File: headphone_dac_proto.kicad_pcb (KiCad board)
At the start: 2 copper layers, 75.5 x 55.5 mm, 61 parts, among them J1 USB_B_Mini, J2 Conn_02x10_Odd_Even, J3 Conn_02x05_Odd_Even, J4 Conn_01x06_Male, J5 Conn_01x06, J6 6.35mm, U1 LT3042xMSE, U2 CY8C5888LTI-LP097, U3 CS4344, U4 TPA6139A2, Y1 Crystal_GND24

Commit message: Change to 4 layer board
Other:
- copper layers 2 -> 4

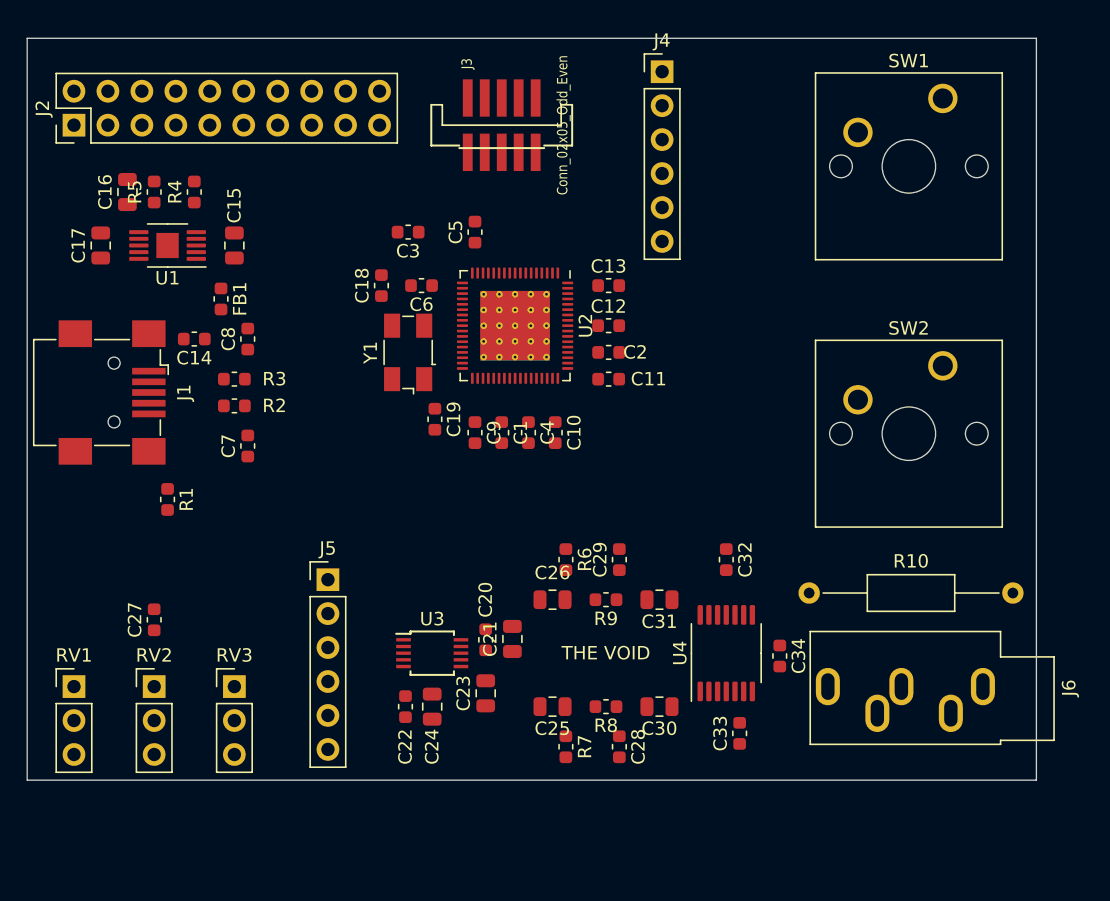
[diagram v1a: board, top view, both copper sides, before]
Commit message: Change peripheral switches and pots
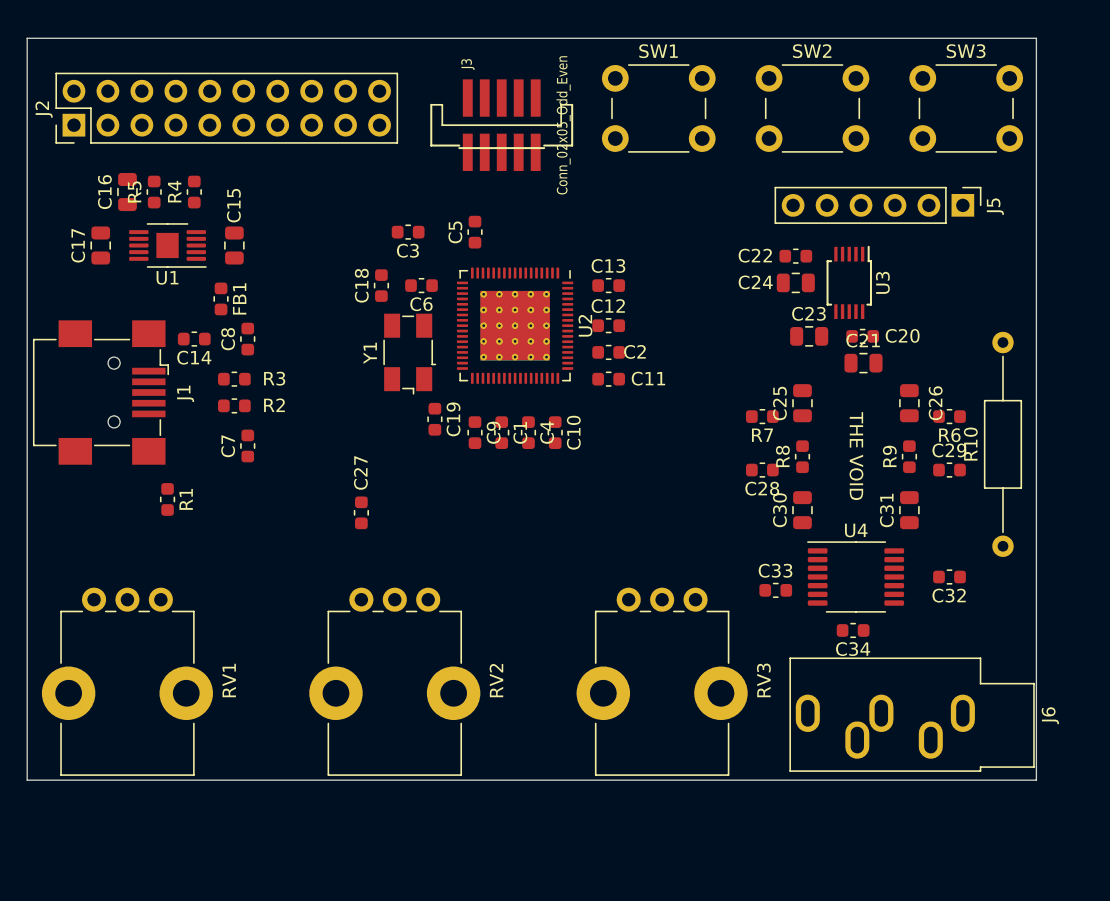
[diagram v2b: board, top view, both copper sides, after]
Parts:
- removed J4: Conn_01x06_Male, Connector_PinHeader_2.54mm:PinHeader_1x06_P2.54mm_Vertical
- added SW3: ~, Button_Switch_THT:SW_PUSH_6mm_H5mm, F.Cu at (155.5, 95.5)
- RV1, RV2, RV3: footprint Connector_PinHeader_2.54mm:PinHeader_1x03_P2.54mm_Vertical -> Potentiometer_THT:Potentiometer_Bourns_PTV09A-1_Single_Vertical
- SW1, SW2: footprint Button_Switch_Keyboard:SW_Cherry_MX_1.00u_PCB -> Button_Switch_THT:SW_PUSH_6mm_H5mm
- moved J5 55.1 mm to (158.5, 105.0), turned to 270 degrees
- moved C22 44.6 mm to (146.0, 108.8), turned to 180 degrees
- moved C24 41.8 mm to (146.0, 110.8), turned to 180 degrees
- moved U3 41.7 mm to (150.0, 110.8), turned to 270 degrees
- moved C20 36.2 mm to (151.0, 114.8), turned to 0 degrees
- moved C23 36.0 mm to (147.0, 114.8), turned to 0 degrees
- moved C21 33.4 mm to (151.1, 116.8), turned to 0 degrees
- moved R6 30.6 mm to (157.5, 120.8), turned to 180 degrees
- moved C26 30.5 mm to (154.5, 119.8), turned to 90 degrees
- moved RV3 30.2 mm to (133.5, 134.5), turned to 270 degrees
- moved C25 29.4 mm to (146.5, 119.8), turned to 90 degrees
- moved R7 28.7 mm to (143.5, 120.8), turned to 180 degrees
- moved C29 25.6 mm to (157.5, 124.8), turned to 0 degrees
- moved SW2 25.1 mm to (144.0, 95.5)
- moved R9 25.1 mm to (154.5, 123.8), turned to 90 degrees
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
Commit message: Change all the things
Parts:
- added C35: 1uF, Capacitor_SMD:C_0603_1608Metric, F.Cu at (113.5, 131.5)
- added C36: 1uF, Capacitor_SMD:C_0603_1608Metric, F.Cu at (133.5, 131.5)
- moved C27 20.3 mm to (93.5, 131.5)
- moved SW1 7.91 mm to (139.0, 100.0), turned to 180 degrees
- moved SW3 7.91 mm to (162.0, 100.0), turned to 180 degrees

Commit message: Placement is complete. Actually though.
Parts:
- added H1: ~, MountingHole:MountingHole_3mm_Pad_Via, F.Cu at (92.0, 151.5)
- added H2: ~, MountingHole:MountingHole_3mm_Pad, F.Cu at (92.0, 96.0)
- added H3: ~, MountingHole:MountingHole_3mm_Pad, F.Cu at (160.5, 96.0)
- added H4: ~, MountingHole:MountingHole_3mm_Pad, F.Cu at (160.5, 151.5)
- SW1, SW2, SW3: footprint Button_Switch_THT:SW_PUSH_6mm_H5mm -> Button_Switch_THT:SW_PUSH_6mm_H13mm
- moved J5 20.7 mm to (139.0, 112.0)
- moved J3 13.4 mm to (114.5, 108.5), turned to 0 degrees
- moved C5 9.82 mm to (119.5, 116.5)
- moved C27 9.22 mm to (99.5, 138.5)
- moved RV1 9.22 mm to (99.5, 141.5)
- moved C1 9.01 mm to (123.5, 131.0)
- moved C10 9.01 mm to (127.5, 131.0)
- moved C11 9.01 mm to (131.5, 127.0)
- moved C12 9.01 mm to (131.5, 123.0)
- moved C13 9.01 mm to (131.5, 120.0)
- moved C18 9.01 mm to (114.5, 120.0)
- moved C19 9.01 mm to (118.5, 130.0)
- moved C2 9.01 mm to (131.5, 125.0)
- moved C3 9.01 mm to (116.5, 116.0)
- moved C4 9.01 mm to (125.5, 131.0)
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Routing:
- added copper zone on In2.Cu, net +3V3
- added copper zone on In1.Cu, net GND
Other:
- board size 75.5 x 55.5 mm -> 75.5 x 62.5 mm

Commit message: I'm sorry Jackson. Please don't read these commit messages
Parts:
- removed J5: Conn_01x06, Connector_PinHeader_2.54mm:PinHeader_1x06_P2.54mm_Vertical
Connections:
- net /i2s_sdi renamed Net-(U2-Pad53)
- SW1 pad 1: Net-(SW1-Pad1) -> /sw1
- SW2 pad 2: Net-(SW2-Pad2) -> /sw2
- SW3 pad 1: Net-(SW3-Pad1) -> /sw3
- U2 pad 1: /bt_rts -> /i2s_sck
- U2 pad 2: /bt_rx -> /i2s_sdo
- U2 pad 3: Net-(SW1-Pad1) -> /sw2
- U2 pad 4: Net-(SW2-Pad2) -> /sw1
- U2 pad 48: /i2s_mck -> Net-(U2-Pad48)
- U2 pad 49: /i2s_lrck -> Net-(U2-Pad49)
- U2 pad 50: /i2s_sck -> Net-(U2-Pad50)
- U2 pad 51: /i2s_sdo -> Net-(U2-Pad51)
- U2 pad 61: Net-(SW3-Pad1) -> Net-(U2-Pad61)
- U2 pad 66: /bt_cts -> /i2s_mck
- U2 pad 68: /bt_tx -> /i2s_lrck
- U3 pad 1: /i2s_sd -> /i2s_sdo

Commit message: Started routing
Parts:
- moved U3 11.8 mm to (138.3, 109.5), turned to 0 degrees
- moved C22 10.8 mm to (136.3, 113.5), turned to 270 degrees
- moved C21 10.8 mm to (144.3, 108.4), turned to 90 degrees
- moved C20 10.7 mm to (142.3, 108.5), turned to 90 degrees
- moved C24 8.16 mm to (138.3, 113.5), turned to 270 degrees
- moved C23 5.23 mm to (142.3, 112.5), turned to 90 degrees
- moved C13 2.26 mm to (131.8, 117.8), turned to 90 degrees
- moved C10 2.25 mm to (125.2, 131.0)
- moved C18 2.14 mm to (116.5, 120.8), turned to 0 degrees
- moved C19 2.14 mm to (116.5, 129.2), turned to 180 degrees
- moved C12 1.60 mm to (132.5, 124.2)
- moved C4 1.50 mm to (127.0, 131.0)
- moved C2 1.41 mm to (132.5, 126.0)
- moved C3 1.27 mm to (116.8, 117.2)
- moved C11 1.25 mm to (132.5, 127.8)
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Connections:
- C27 pad 1: Net-(C27-Pad1) -> /as
- C35 pad 1: Net-(C27-Pad1) -> /as
- C36 pad 1: Net-(C27-Pad1) -> /as
- RV1 pad 1: Net-(C27-Pad1) -> /as
- RV2 pad 1: Net-(C27-Pad1) -> /as
- RV3 pad 1: Net-(C27-Pad1) -> /as
- U2 pad 3: /sw2 -> /bt_tx
- U2 pad 33: /a2 -> /as
- U2 pad 34: /a1 -> /a0
- U2 pad 36: /a0 -> /a1
- U2 pad 37: Net-(C27-Pad1) -> /a2
- U2 pad 4: /sw1 -> /bt_rx
- U2 pad 61: Net-(U2-Pad61) -> /bt_cts
- U2 pad 62: /ft_~rts~ -> /bt_rts
- U2 pad 63: /ft_rx -> /sw3
- U2 pad 64: /ft_tx -> /sw2
- U2 pad 65: /ft_~cts~ -> /sw1
- U4 pad 8: Net-(U4-Pad7) -> Net-(U4-Pad8)
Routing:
- net /sw3: track 0.00 -> 39.6 mm, vias 0 -> 1
- net /bt_cts: track 0.00 -> 38.4 mm, vias 0 -> 1
- net /bt_rts: track 0.00 -> 37.8 mm, vias 0 -> 1
- net +3V3: track 0.00 -> 37.1 mm, vias 0 -> 5
- net GND: track 0.00 -> 35.6 mm, vias 0 -> 1
- net /bt_rx: track 0.00 -> 32.5 mm
- net /bt_tx: track 0.00 -> 30.6 mm
- net /sw2: track 0.00 -> 28.6 mm, vias 0 -> 1
- net /sw1: track 0.00 -> 27.8 mm, vias 0 -> 1
- net /~mute~: track 0.00 -> 24.5 mm
- net /vccd: track 0.00 -> 20.0 mm, vias 0 -> 2
- net /usb_d+: track 0.00 -> 18.1 mm, vias 0 -> 2
- net /usb_d-: track 0.00 -> 17.3 mm, vias 0 -> 2
- net /i2s_mck: track 0.00 -> 17.1 mm
- net /i2s_sdo: track 0.00 -> 14.9 mm
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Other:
- net class Default: trace_width 0.25 -> 0.2; via_dia 0.8 -> 0.6; via_drill 0.4 -> 0.3
- rule pad_to_mask_clearance: 0.05 -> 0.038
- rule trace_min: 0.2 -> 0.15
- rule via_min_size: 0.4 -> 0.6

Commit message: ERC and DRC passing
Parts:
- U1: footprint Package_SO:MSOP-10-1EP_3x3mm_P0.5mm_EP1.68x1.88mm -> Package_SO:MSOP-10-1EP_3x3mm_P0.5mm_EP1.68x1.88mm_ThermalVias
- moved R6 14.0 mm to (143.5, 120.8), turned to 0 degrees
- moved R7 13.8 mm to (157.2, 120.8), turned to 0 degrees
- moved R5 4.25 mm to (94.2, 106.0)
- moved C16 4.14 mm to (92.2, 105.8)
- moved C32 2.44 mm to (155.8, 134.5), turned to 90 degrees
- moved C27 2.06 mm to (101.5, 139.0), turned to 0 degrees
- moved J3 2.02 mm to (113.5, 110.2)
- moved C9 1.80 mm to (120.8, 129.5)
- moved C23 1.72 mm to (140.8, 113.2)
- moved FB1 1.35 mm to (101.8, 112.5)
- moved C17 1.25 mm to (94.0, 109.2), turned to 180 degrees
- moved C33 1.22 mm to (145.5, 134.5), turned to 90 degrees
- turned C28 to 0 degrees
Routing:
- net /as: track 0.00 -> 72.5 mm
- net GND: track 35.6 -> 102.6 mm, vias 1 -> 41
- net +3V3: track 37.1 -> 74.5 mm, vias 5 -> 12
- net Net-(J6-PadT): track 0.00 -> 28.3 mm
- net /a2: track 0.00 -> 27.2 mm
- net /a0: track 0.00 -> 26.4 mm
- net /xres: track 0.00 -> 26.1 mm
- net Net-(J1-Pad6): track 0.00 -> 23.2 mm
- net Net-(J6-PadR): track 0.00 -> 23.1 mm
- net Net-(C26-Pad2): track 0.00 -> 21.8 mm
- net /tms: track 0.00 -> 16.3 mm
- net /a1: track 0.00 -> 15.7 mm
- net /tck: track 0.00 -> 15.3 mm
- net /tdo: track 0.00 -> 14.0 mm
- net /tdi: track 0.00 -> 12.9 mm
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- added copper zone on F.Cu, net +3V3
- added copper zone on F.Cu, net +5V
- added copper zone on B.Cu, net GND

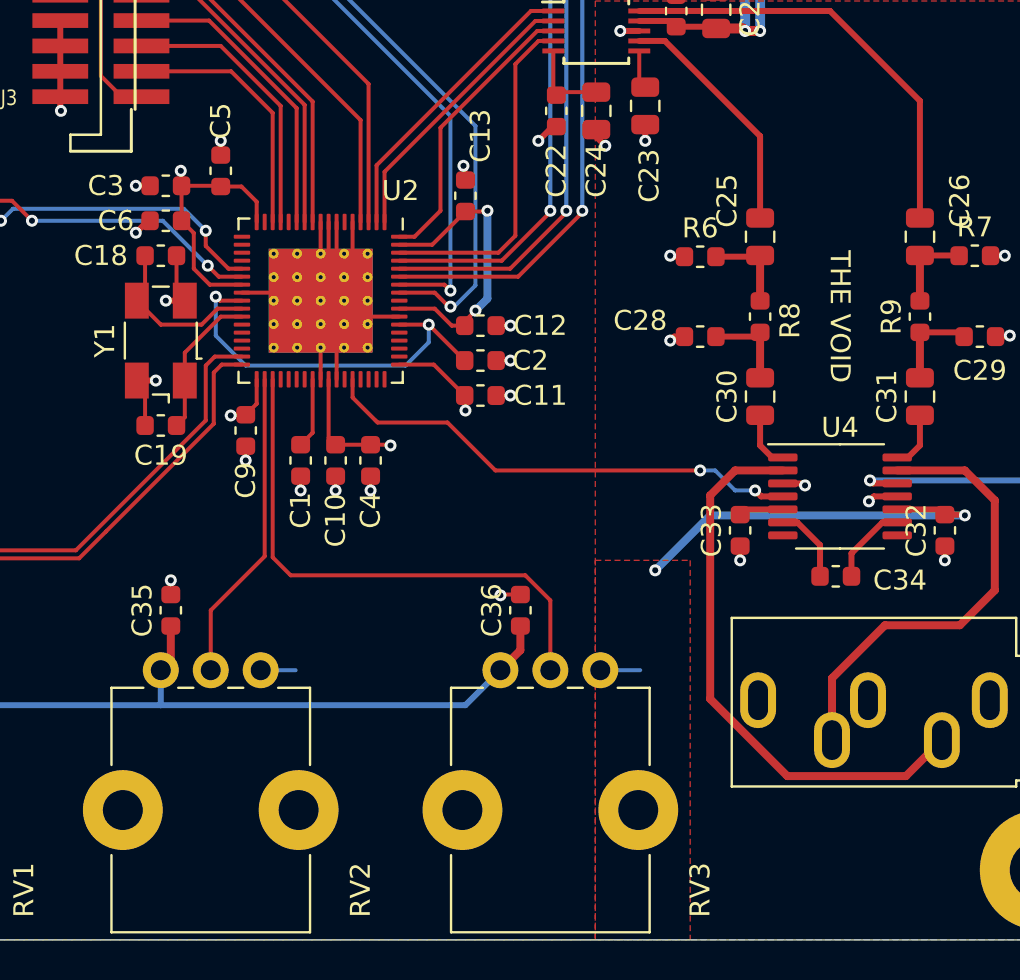
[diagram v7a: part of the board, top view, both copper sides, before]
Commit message: Switch to two layers. ERC, DRC passing agaom
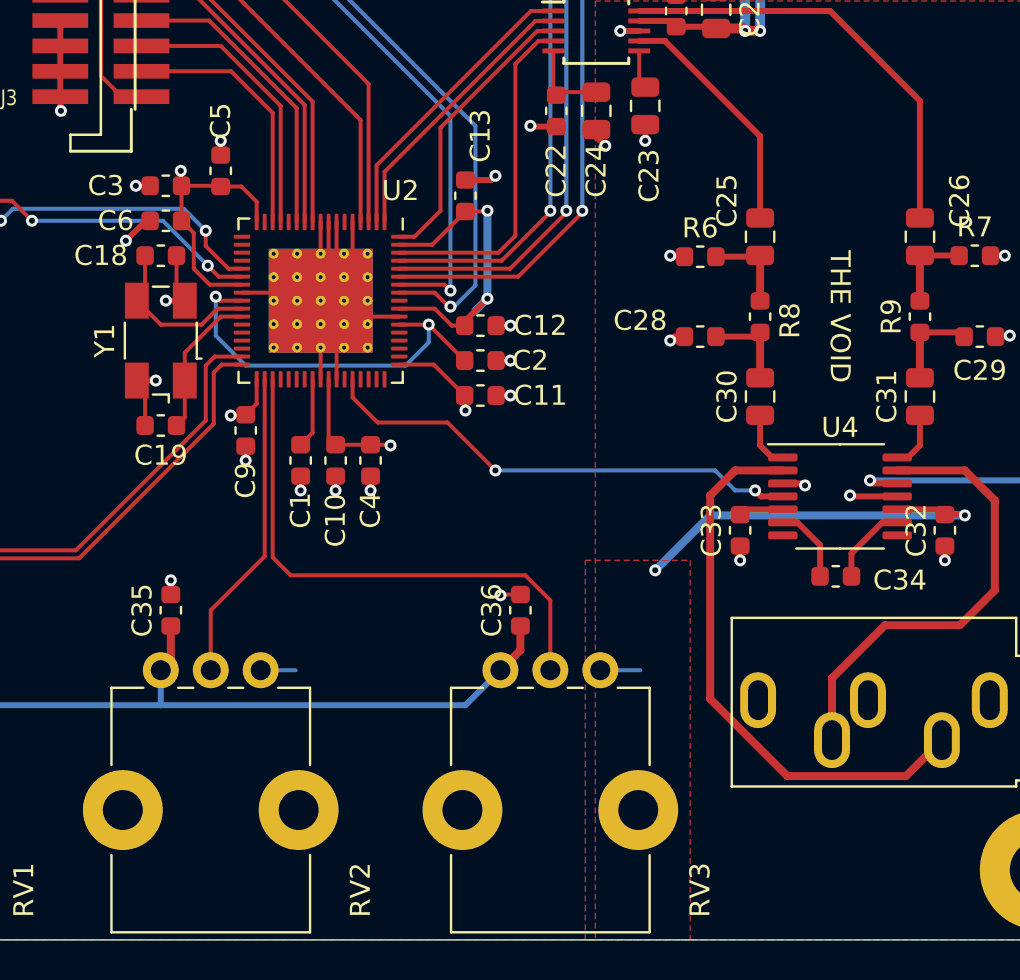
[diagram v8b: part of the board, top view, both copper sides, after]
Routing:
- net GND: track 102.6 -> 105.3 mm
- net +3V3: track 74.5 -> 76.2 mm
- removed copper zone on In2.Cu, net +3V3
- removed copper zone on In1.Cu, net GND
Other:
- copper layers 4 -> 2
